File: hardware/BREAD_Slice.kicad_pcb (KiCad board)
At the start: 2 copper layers, 70 x 100 mm, 40 parts, among them J1 I2C_01x04, J2 Conn_01x10_Female, J3 Screw_Terminal_01x02, J4 Screw_Terminal_01x02, J5 Screw_Terminal_01x02, J6 Screw_Terminal_01x02, J7 Screw_Terminal_01x02, J8 Screw_Terminal_01x02, Q1 TIP120, Q2 TIP120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

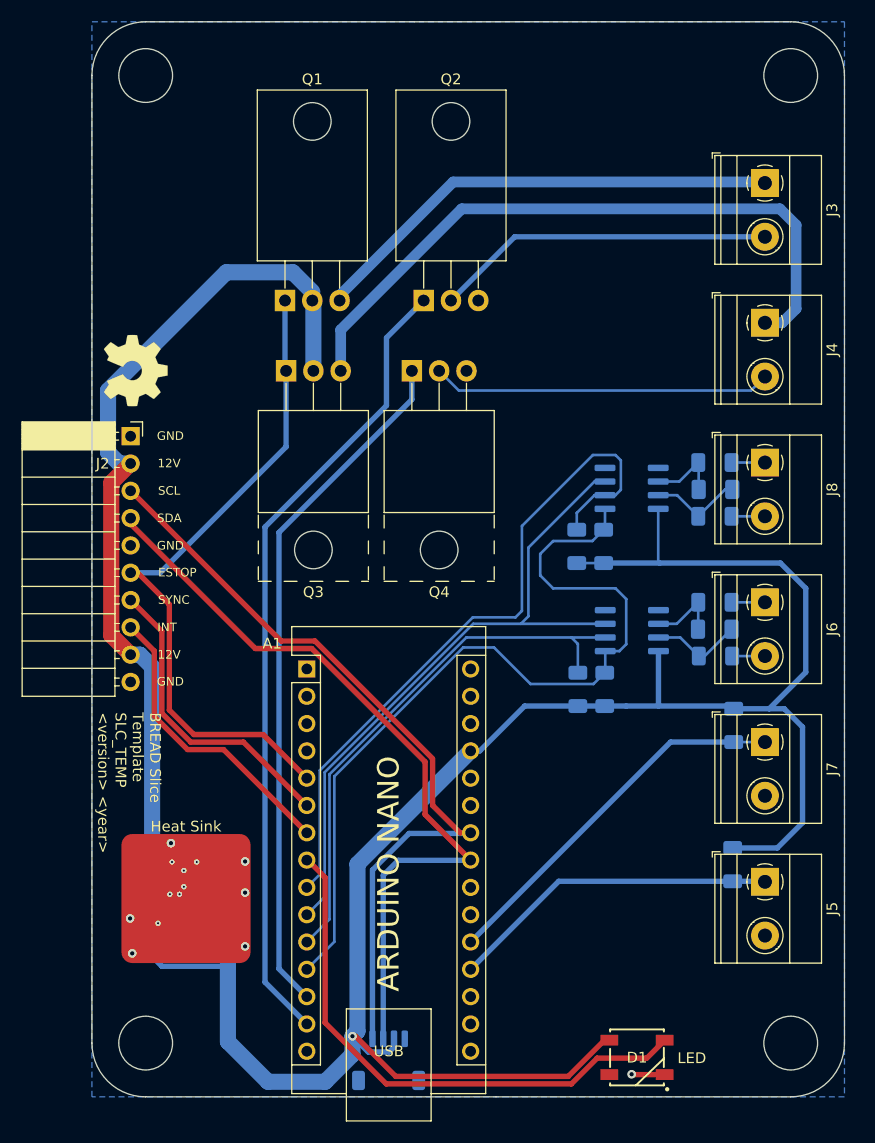
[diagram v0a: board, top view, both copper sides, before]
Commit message: updated to the correct terminals and proper hierarchial pages
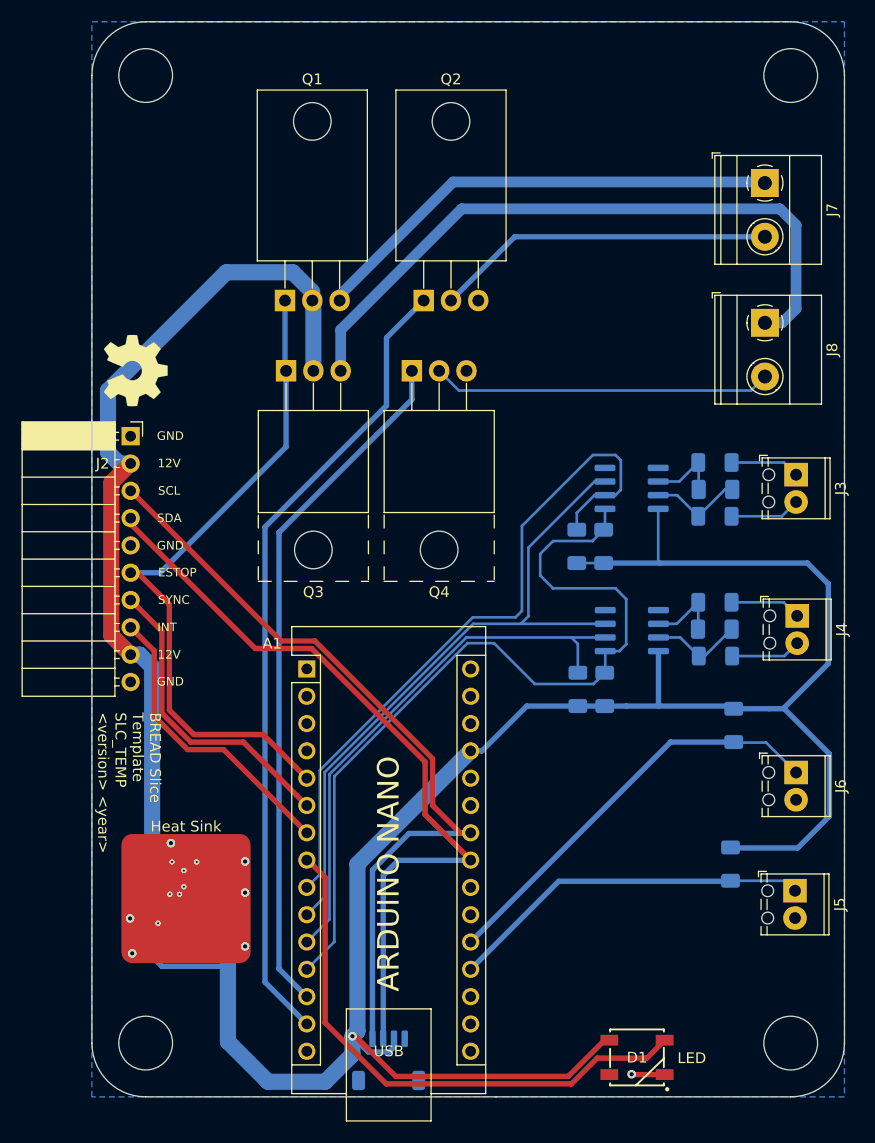
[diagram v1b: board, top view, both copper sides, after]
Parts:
- removed the J7 at (185.2, 106.8)
- removed the J8 at (185.2, 80.8)
- removed the R3 at (182.2, 118.2)
- removed the R6 at (182.3, 105.2)
- added J3: Screw_Terminal_01x02, TerminalBlock_Phoenix:TerminalBlock_Phoenix_MPT-0,5-2-2.54_1x02_P2.54mm_Horizontal, F.Cu at (188.1, 81.9)
- added J4: Screw_Terminal_01x02, TerminalBlock_Phoenix:TerminalBlock_Phoenix_MPT-0,5-2-2.54_1x02_P2.54mm_Horizontal, F.Cu at (188.2, 95.1)
- added R1: 10k, Resistor_SMD:R_1206_3216Metric_Pad1.30x1.75mm_HandSolder, B.Cu at (182.0, 118.2)
- added R2: 10k, Resistor_SMD:R_1206_3216Metric_Pad1.30x1.75mm_HandSolder, B.Cu at (182.3, 105.2)
- J5, J6: footprint TerminalBlock_Phoenix:TerminalBlock_Phoenix_MKDS-1,5-2_1x02_P5.00mm_Horizontal -> TerminalBlock_Phoenix:TerminalBlock_Phoenix_MPT-0,5-2-2.54_1x02_P2.54mm_Horizontal
- moved J6 16.1 mm to (188.1, 109.6)
- moved J5 2.92 mm to (188.0, 120.6)
- renumbered J3 to J7, J4 to J8, R1 to R3, R2 to R4, R4 to R5, R5 to R6
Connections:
- FB1 pad 2: Net-(J6-Pin_2) -> /MAX31855K/T+
- FB2 pad 2: Net-(J6-Pin_1) -> /MAX31855K/T-
- FB3 pad 2: Net-(J8-Pin_2) (its old number) -> /MAX31855K1/T+
- FB4 pad 2: Net-(J8-Pin_1) (its old number) -> /MAX31855K1/T-
- J6 pad 1: Net-(J6-Pin_1) -> /TMSTR2
- J6 pad 2: Net-(J6-Pin_2) -> GND
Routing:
- net /MAX31855K/T-: track 0.00 -> 6.62 mm
- net /MAX31855K1/T+: track 0.00 -> 6.55 mm
- net /MAX31855K/T+: track 0.00 -> 6.55 mm
- net /MAX31855K1/T-: track 0.00 -> 6.47 mm
- net +5V: track 203.5 -> 209.3 mm
- net /TMSTR2: track 35.1 -> 39.1 mm
- net /TMSTR1: track 30.8 -> 34.1 mm
- net Net-(J8-Pin_2) (its old number): track 3.11 -> 0.00 mm
- net Net-(J8-Pin_1) (its old number): track 3.11 -> 0.00 mm
- net Net-(J6-Pin_1): track 3.11 -> 0.00 mm
- net Net-(J6-Pin_2): track 3.06 -> 0.00 mm

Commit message: JLCPCB order rev-A
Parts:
- added J10: Term_PressFit_1x01_5mm_Phoenix_Contact_1751066, KML-Custom:1751066, F.Cu at (188.0, 102.1)
- added J11: Term_PressFit_1x01_5mm_Phoenix_Contact_1751066, KML-Custom:1751066, F.Cu at (187.9, 57.2)
- added J12: Term_PressFit_1x01_5mm_Phoenix_Contact_1751066, KML-Custom:1751066, F.Cu at (187.9, 66.0)
- added J13: Term_PressFit_1x01_5mm_Phoenix_Contact_1751066, KML-Custom:1751066, F.Cu at (187.9, 61.6)
- added J14: Term_PressFit_1x01_5mm_Phoenix_Contact_1751066, KML-Custom:1751066, F.Cu at (187.9, 70.4)
- added J9: Term_PressFit_1x01_5mm_Phoenix_Contact_1751066, KML-Custom:1751066, F.Cu at (188.0, 106.5)
- J3, J4, J5, J6: value Screw_Terminal_01x02 -> Term_PressFit_1x01_5mm_Phoenix_Contact_1751066; footprint TerminalBlock_Phoenix:TerminalBlock_Phoenix_MPT-0,5-2-2.54_1x02_P2.54mm_Horizontal -> KML-Custom:1751066
- J7, J8: value Screw_Terminal_01x02 -> Term_PressFit_1x01_5mm_Phoenix_Contact_1751066; footprint TerminalBlock_Phoenix:TerminalBlock_Phoenix_MKDS-1,5-2_1x02_P5.00mm_Horizontal -> KML-Custom:1751066
- moved J7 60.6 mm to (188.0, 115.3), turned to 90 degrees
- moved J8 43.2 mm to (188.0, 110.9), turned to 90 degrees
- moved J5 31.7 mm to (188.0, 88.9), turned to 90 degrees
- moved J6 25.1 mm to (188.0, 84.5), turned to 90 degrees
- moved J3 15.8 mm to (188.0, 97.7), turned to 90 degrees
- moved C5 7.07 mm to (173.9, 98.8)
- moved C6 7.07 mm to (174.0, 85.8)
- moved FB1 7.07 mm to (174.0, 101.3)
- moved FB2 7.07 mm to (173.9, 96.3)
- moved FB3 7.07 mm to (173.9, 88.3)
- moved FB4 7.07 mm to (173.9, 83.3)
- moved R2 7.07 mm to (175.7, 107.7)
- moved U2 7.07 mm to (166.2, 98.9)
- moved U3 7.07 mm to (166.2, 85.7)
- moved R1 6.43 mm to (175.7, 116.8), turned to 90 degrees
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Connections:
- J3 pad 1: /MAX31855K1/T- -> /MAX31855K/T+
- J3 pad 2: /MAX31855K1/T+ -> /MAX31855K/T+
- J4 pad 2: /MAX31855K/T+ -> /MAX31855K/T-
- J5 pad 1: /TMSTR1 -> /MAX31855K1/T+
- J5 pad 2: GND -> /MAX31855K1/T+
- J6 pad 1: /TMSTR2 -> /MAX31855K1/T-
- J6 pad 2: GND -> /MAX31855K1/T-
- J7 pad 1: Net-(J7-Pin_1) -> /TMSTR1
- J7 pad 2: Net-(J7-Pin_2) -> /TMSTR1
- J8 pad 1: Net-(J8-Pin_1) -> GND
- J8 pad 2: Net-(J8-Pin_2) -> GND
- Q1 pad 3: Net-(J7-Pin_1) -> Net-(Q1-E)
- Q2 pad 2: Net-(J7-Pin_2) -> Net-(Q2-C)
- Q3 pad 3: Net-(J8-Pin_1) -> Net-(Q3-E)
- Q4 pad 2: Net-(J8-Pin_2) -> Net-(Q4-C)
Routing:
- net Net-(J8-Pin_1): track 62.8 -> 0.00 mm
- net Net-(Q3-E): track 0.00 -> 51.3 mm
- net Net-(Q1-E): track 0.00 -> 48.4 mm
- net Net-(J7-Pin_1): track 44.4 -> 0.00 mm
- net +5V: track 209.3 -> 170.9 mm, vias 1 -> 2
- net Net-(Q4-C): track 0.00 -> 35.1 mm
- net Net-(Q2-C): track 0.00 -> 33.4 mm
- net Net-(J7-Pin_2): track 31.7 -> 0.00 mm
- net Net-(J8-Pin_2): track 31.6 -> 0.00 mm
- net GND: track 19.6 -> 36.0 mm
- net /DATA: track 62.8 -> 53.4 mm
- net /MAX31855K/T+: track 6.55 -> 14.0 mm
- net /MAX31855K/T-: track 6.62 -> 13.8 mm
- net /MAX31855K1/T-: track 6.47 -> 13.1 mm
- net /MAX31855K1/T+: track 6.55 -> 12.8 mm
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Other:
- board text added: "BREAD Slice DC Header (SLC_HEAT) Cam K Brooks rev.A [09-2024]"
- board text removed: "BREAD Slice Template SLC_TEMP <version> <year>"
